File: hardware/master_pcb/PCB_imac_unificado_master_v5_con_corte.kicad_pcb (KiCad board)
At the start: 2 copper layers, 251.9 x 267 mm, 17 parts

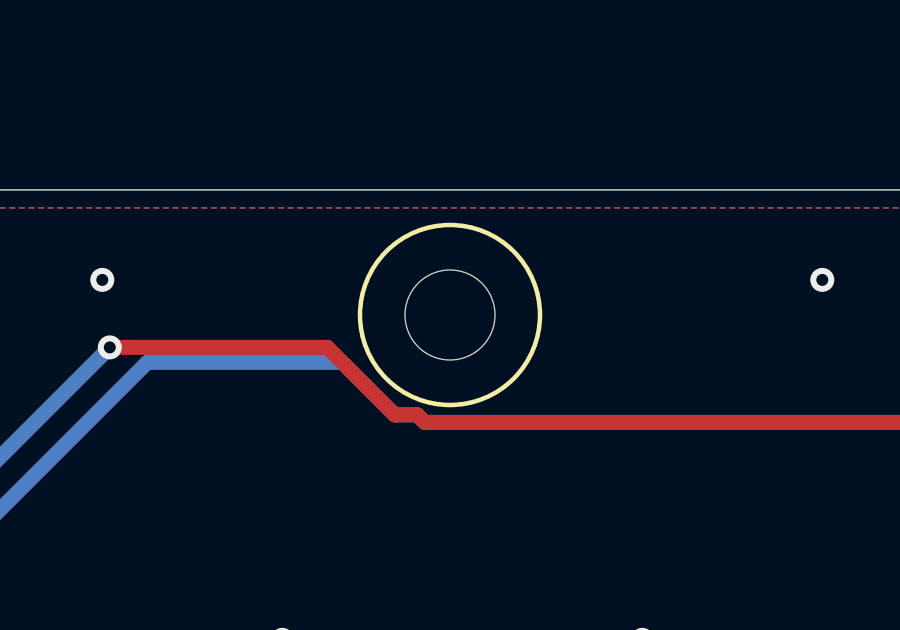
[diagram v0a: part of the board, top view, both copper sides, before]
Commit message: Master: biblioteca JJaroll con huellas normalizadas (DRC 7 avisos de biblioteca)
Co-Authored-By: Claude Sonnet 5.5 <noreply@anthropic.com>
Claude-Session: https://claude.ai/code/session_01CUq9b9AsuT1a2cpCUYrCH3
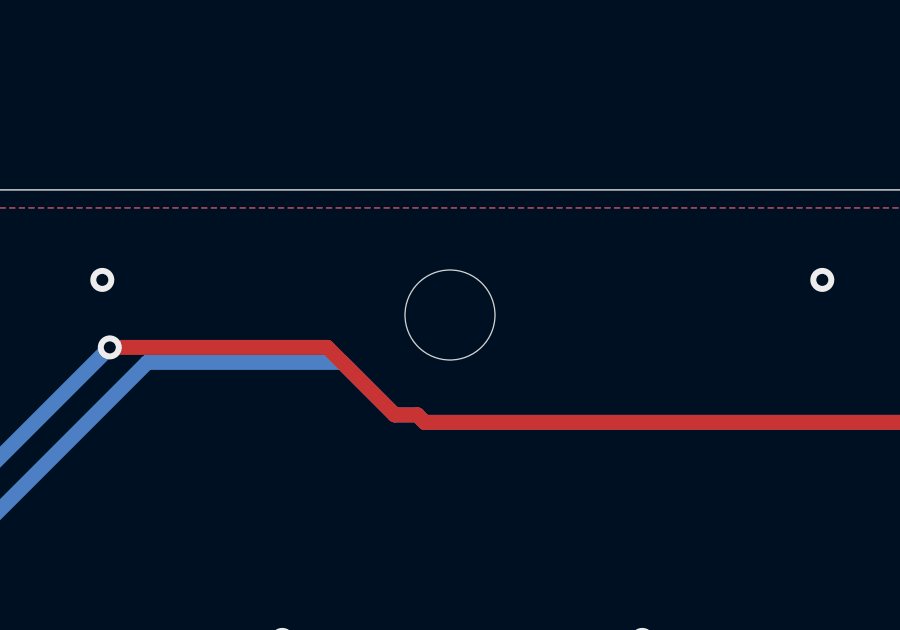
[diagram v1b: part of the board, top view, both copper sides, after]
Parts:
- T_J22_J2: footprint JJaroll:TerminalBlock_Phoenix_PT-1,5-10-5.0-H_1x10_P5.00mm_Horizontal -> JJaroll:TerminalBlock_Phoenix_PT-1,5-10-5.0-H_1x10_P5.00mm_Horizontal_J22
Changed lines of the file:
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@@
 		(embedded_fonts no)
 	)
-	(footprint "JJaroll:TerminalBlock_Phoenix_PT-1,5-10-5.0-H_1x10_P5.00mm_Horizontal"
+	(footprint "JJaroll:TerminalBlock_Phoenix_PT-1,5-10-5.0-H_1x10_P5.00mm_Horizontal_J22"
 		(layer "F.Cu")
 		(at 60.296 275.429 90)
@@
 		(fp_circle
 			(center 0 0)
-			(end 3 0)
-			(stroke
-				(width 0.15)
-				(type solid)
-			)
-			(fill no)
-			(layer "F.SilkS")
-		)
-		(fp_circle
-			(center 0 0)
